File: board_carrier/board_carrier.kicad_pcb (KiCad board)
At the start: 2 copper layers, 40 x 36.5 mm, 13 parts, among them J1 Conn_01x08, J2 Conn_01x08, J3 Conn_02x06_Top_Bottom, U1 TJA1051T-3, U2 LM78M05_TO252

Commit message: carrier mods
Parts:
- removed the REF** at (45.0, 66.8)
- added REF**: OSHW-Logo_11.4x12mm_SilkScreen, Symbol:OSHW-Logo_11.4x12mm_SilkScreen, B.Cu at (60.0, 83.0)
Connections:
- J3 pad 10: Net-(J3-Pad10) -> /LSU_Un
- J3 pad 7: /LSU_Vm -> Net-(J3-Pad7)
- J3 pad 8: /LSU_Rtrim -> /LSU_Vm
- J3 pad 9: /LSU_Un -> /LSU_Rtrim
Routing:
- net /LSU_Vm: track 26.2 -> 32.2 mm
- net /LSU_Rtrim: track 35.3 -> 40.0 mm
- net /LSU_Un: track 43.2 -> 47.9 mm
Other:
- board text added: "5v"
- board text added: "Boot0"
- board text added: "CAN RX"
- board text added: "CAN TX"
- board text added: "Heater-"
- board text added: "Ip 1"
- board text added: "RX"
- board text added: "Rtrim 5"
- board text added: "TX"
- board text added: "Un 6"
- board text added: "Vm 2"
- board text added: "nRESET"

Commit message: carrier probably done
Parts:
- added JLCTAG**: JLC_PCB_TAG, rusefi:JLC_PCB_TAG, F.Cu at (50.6, 56.4)
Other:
- board text added: "v1.0"
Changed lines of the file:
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@@
   (general
     (thickness 1.6)
-    (drawings 46)
+    (drawings 47)
     (tracks 123)
     (zones 0)
-    (modules 13)
+    (modules 14)
     (nets 21)
   )
@@
     (add_net "Net-(J3-Pad5)")
     (add_net "Net-(J3-Pad7)")
+  )
+  (module rusefi:JLC_PCB_TAG (layer F.Cu)
+    (at 50.6 56.4)
+    (fp_text reference JLCTAG** (at 0 0.5) (layer F.SilkS) hide
+      (effects (font (size 1 1) (thickness 0.15)))
+    )
+    (fp_text value JLC_PCB_TAG (at 0 -0.5) (layer F.Fab)
+      (effects (font (size 1 1) (thickness 0.15)))
+    )
+    (fp_line (start 0 0) (end 19.05 0) (layer F.SilkS) (width 0.12))
+    (fp_line (start 19.05 0) (end 19.05 3.81) (layer F.SilkS) (width 0.12))
+    (fp_line (start 19.05 3.81) (end 0 3.81) (layer F.SilkS) (width 0.12))
+    (fp_line (start 0 3.81) (end 0 0) (layer F.SilkS) (width 0.12))
+    (fp_text user "JLC Order Number" (at 9.525 0.635) (layer F.SilkS)
+      (effects (font (size 0.762 0.762) (thickness 0.127)))
+    )
+    (fp_text user JLCJLCJLCJLC (at 9.525 2.54) (layer F.SilkS)
+      (effects (font (size 1.524 1.524) (thickness 0.2032)))
+    )
   )
   (module Symbol:OSHW-Logo_11.4x12mm_SilkScreen (layer B.Cu)
@@
     )
   )
+  (gr_text v1.0 (at 44.4 66.2) (layer B.SilkS)
+    (effects (font (size 1 1) (thickness 0.15)) (justify mirror))
+  )
   (gr_text 5v (at 45 71.2) (layer B.SilkS)

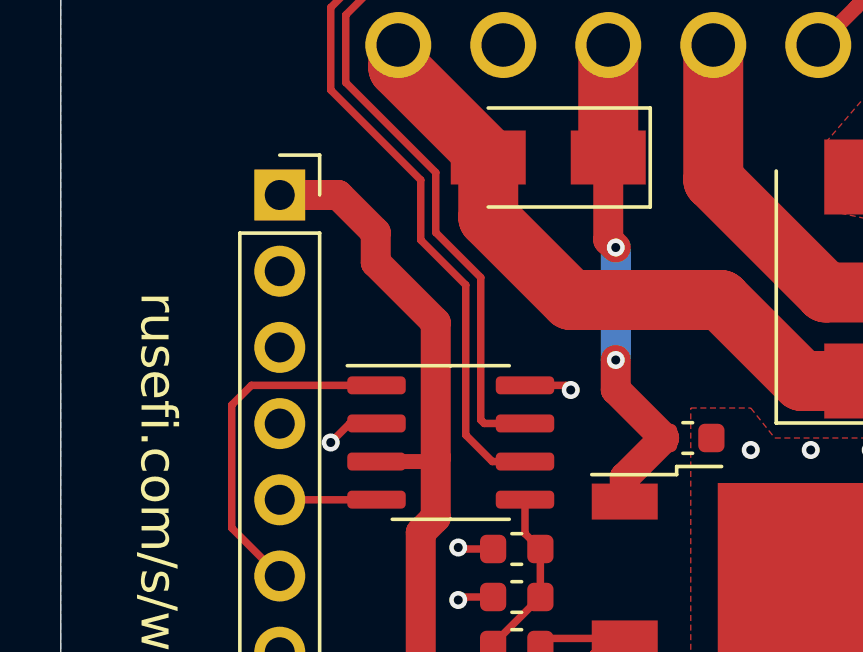
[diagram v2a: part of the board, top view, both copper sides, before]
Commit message: add CAN caps, solid reg pad
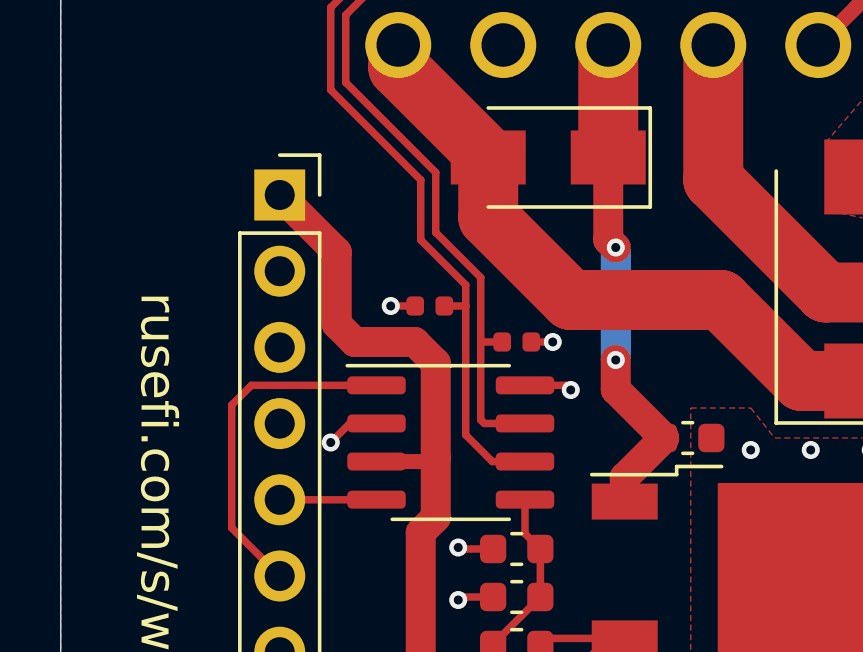
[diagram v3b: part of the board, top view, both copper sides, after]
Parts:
- added C4: 47p, Capacitor_SMD:C_0402_1005Metric, F.Cu at (55.2, 75.9)
- added C5: 47p, Capacitor_SMD:C_0402_1005Metric, F.Cu at (52.3, 74.7)
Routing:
- net GND: track 5.76 -> 7.29 mm, vias 16 -> 18
- net /CAN_L: track 21.6 -> 22.4 mm
- net /CAN_H: track 23.2 -> 23.9 mm

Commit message: moar caps
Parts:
- added C10: 10u, Capacitor_SMD:C_1206_3216Metric, F.Cu at (61.7, 77.1)
- added C6: 22u, Capacitor_SMD:C_0805_2012Metric, F.Cu at (58.8, 89.8)
- added C7: 10u, Capacitor_SMD:C_1206_3216Metric, F.Cu at (53.2, 72.4)
- added C8: 10u, Capacitor_SMD:C_1206_3216Metric, F.Cu at (53.2, 70.0)
- added C9: 10u, Capacitor_SMD:C_1206_3216Metric, F.Cu at (53.2, 74.8)
- moved C5 3.59 mm to (53.8, 78.0)
- moved D1 3.06 mm to (65.4, 71.2), turned to 0 degrees
- moved D2 2.43 mm to (58.2, 71.2), turned to 270 degrees
- moved C4 2.15 mm to (55.8, 78.0)
- moved C3 2.09 mm to (55.7, 86.4)
- moved R1 2.09 mm to (55.7, 88.0)
- moved R2 2.09 mm to (55.7, 84.8)
- moved U1 2.03 mm to (53.0, 81.3)
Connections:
- J1 pad 3: /UART_TX -> (no net)
- J1 pad 4: /UART_RX -> (no net)
- J1 pad 7: /nRESET -> (no net)
- J1 pad 8: /Boot0 -> (no net)
- J3 pad 5: Net-(J3-Pad5) -> (no net)
- J3 pad 7: Net-(J3-Pad7) -> (no net)
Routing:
- net 12V_RAW: track 22.1 -> 0.00 mm
- net /CAN_L: track 22.4 -> 27.4 mm
- net /CAN_H: track 23.9 -> 28.4 mm
- net /LSU_Heater+: track 16.5 -> 19.6 mm
- net GND: track 7.29 -> 9.40 mm, vias 18 -> 28
- net /CAN_TX: track 11.5 -> 9.37 mm
- net /CAN_RX: track 3.23 -> 4.17 mm
- added copper zone on F.Cu, net 12V_RAW

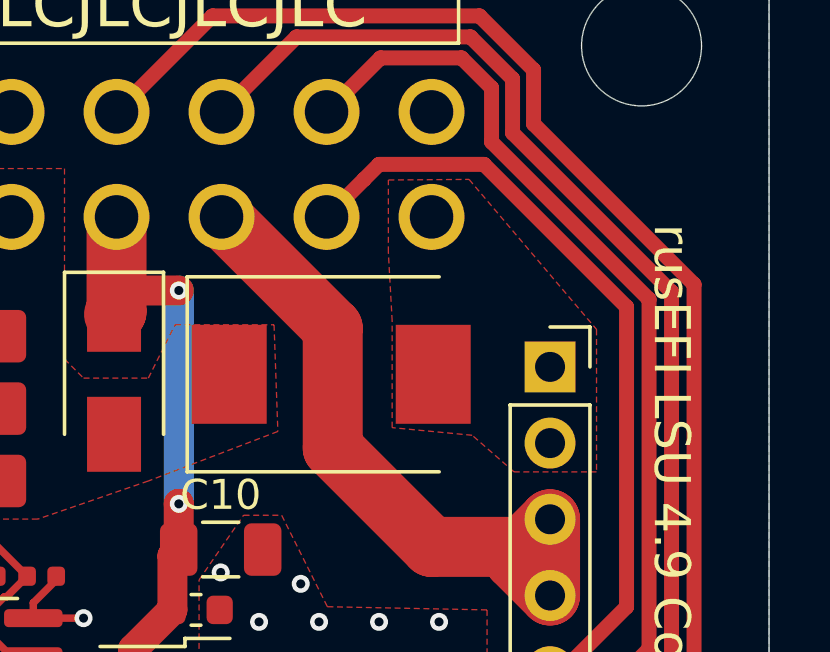
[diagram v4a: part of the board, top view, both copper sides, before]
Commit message: more stitching
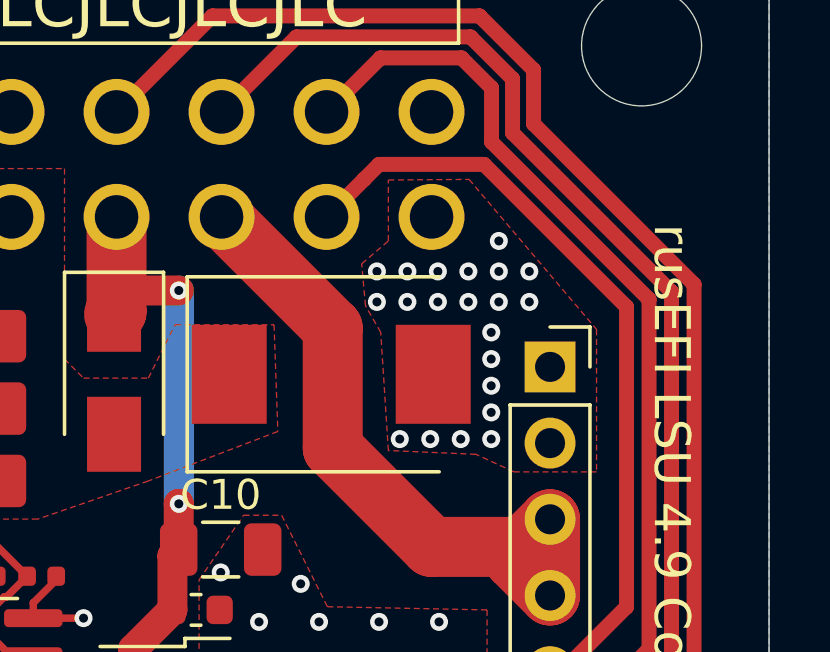
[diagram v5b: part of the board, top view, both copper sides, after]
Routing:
- net GND: vias 28 -> 49
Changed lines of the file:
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@@
     (thickness 1.6)
     (drawings 46)
-    (tracks 156)
+    (tracks 177)
     (zones 0)
     (modules 21)
@@
     (uvia_drill 0.3)
     (add_net +5V)
+    (add_net /Boot0)
     (add_net /CAN_H)
     (add_net /CAN_L)
@@
     (add_net /LSU_Un)
     (add_net /LSU_Vm)
+    (add_net /UART_RX)
+    (add_net /UART_TX)
+    (add_net /nRESET)
     (add_net 12V_RAW)
     (add_net GND)
     (add_net "Net-(C3-Pad1)")
+    (add_net "Net-(J3-Pad5)")
+    (add_net "Net-(J3-Pad7)")
+  )
+  (module Diode_SMD:D_SMA (layer F.Cu)
+    (at 58.166 71.247 270)
+    (descr "Diode SMA (DO-214AC)")
+    (tags "Diode SMA (DO-214AC)")
+    (attr smd)
+    (fp_text reference D2 (at 0 -2.5 90) (layer F.SilkS) hide
+      (effects (font (size 1 1) (thickness 0.15)))
+    )
+    (fp_text value D_Schottky (at 0 2.6 90) (layer F.Fab)
+      (effects (font (size 1 1) (thickness 0.15)))
+    )
+    (fp_line (start -3.4 -1.65) (end 2 -1.65) (layer F.SilkS) (width 0.12))
+    (fp_line (start -3.4 1.65) (end 2 1.65) (layer F.SilkS) (width 0.12))
+    (fp_line (start -0.64944 0.00102) (end 0.50118 -0.79908) (layer F.Fab) (width 0.1))
+    (fp_line (start -0.64944 0.00102) (end 0.50118 0.75032) (layer F.Fab) (width 0.1))
+    (fp_line (start 0.50118 0.75032) (end 0.50118 -0.79908) (layer F.Fab) (width 0.1))
+    (fp_line (start -0.64944 -0.79908) (end -0.64944 0.80112) (layer F.Fab) (width 0.1))
+    (fp_line (start 0.50118 0.00102) (end 1.4994 0.00102) (layer F.Fab) (width 0.1))
+    (fp_line (start -0.64944 0.00102) (end -1.55114 0.00102) (layer F.Fab) (width 0.1))
+    (fp_line (start -3.5 1.75) (end -3.5 -1.75) (layer F.CrtYd) (width 0.05))
+    (fp_line (start 3.5 1.75) (end -3.5 1.75) (layer F.CrtYd) (width 0.05))
+    (fp_line (start 3.5 -1.75) (end 3.5 1.75) (layer F.CrtYd) (width 0.05))
+    (fp_line (start -3.5 -1.75) (end 3.5 -1.75) (layer F.CrtYd) (width 0.05))
+    (fp_line (start 2.3 -1.5) (end -2.3 -1.5) (layer F.Fab) (width 0.1))
+    (fp_line (start 2.3 -1.5) (end 2.3 1.5) (layer F.Fab) (width 0.1))
+    (fp_line (start -2.3 1.5) (end -2.3 -1.5) (layer F.Fab) (width 0.1))
+    (fp_line (start 2.3 1.5) (end -2.3 1.5) (layer F.Fab) (width 0.1))
+    (fp_line (start -3.4 -1.65) (end -3.4 1.65) (layer F.SilkS) (width 0.12))
+    (fp_text user %R (at 0 -2.5 90) (layer F.Fab) hide
+      (effects (font (size 1 1) (thickness 0.15)))
+    )
+    (pad 2 smd rect (at 2 0 270) (size 2.5 1.8) (layers F.Cu F.Paste F.Mask)
+      (net 4 12V_RAW))
+    (pad 1 smd rect (at -2 0 270) (size 2.5 1.8) (layers F.Cu F.Paste F.Mask)
+      (net 9 /LSU_Heater+))
+    (model ${KISYS3DMOD}/Diode_SMD.3dshapes/D_SMA.wrl
+      (at (xyz 0 0 0))
+      (scale (xyz 1 1 1))
+      (rotate (xyz 0 0 0))
+    )
   )
   (module Capacitor_SMD:C_1206_3216Metric (layer F.Cu)
@@
     )
   )
-  (module Diode_SMD:D_SMA (layer F.Cu)
-    (at 58.166 71.247 270)
-    (descr "Diode SMA (DO-214AC)")
-    (tags "Diode SMA (DO-214AC)")
-    (attr smd)
-    (fp_text reference D2 (at 0 -2.5 90) (layer F.SilkS) hide
-      (effects (font (size 1 1) (thickness 0.15)))
-    )
-    (fp_text value D_Schottky (at 0 2.6 90) (layer F.Fab)
-      (effects (font (size 1 1) (thickness 0.15)))
-    )
-    (fp_line (start -3.4 -1.65) (end 2 -1.65) (layer F.SilkS) (width 0.12))
-    (fp_line (start -3.4 1.65) (end 2 1.65) (layer F.SilkS) (width 0.12))
-    (fp_line (start -0.64944 0.00102) (end 0.50118 -0.79908) (layer F.Fab) (width 0.1))
-    (fp_line (start -0.64944 0.00102) (end 0.50118 0.75032) (layer F.Fab) (width 0.1))
-    (fp_line (start 0.50118 0.75032) (end 0.50118 -0.79908) (layer F.Fab) (width 0.1))
-    (fp_line (start -0.64944 -0.79908) (end -0.64944 0.80112) (layer F.Fab) (width 0.1))
-    (fp_line (start 0.50118 0.00102) (end 1.4994 0.00102) (layer F.Fab) (width 0.1))
-    (fp_line (start -0.64944 0.00102) (end -1.55114 0.00102) (layer F.Fab) (width 0.1))
-    (fp_line (start -3.5 1.75) (end -3.5 -1.75) (layer F.CrtYd) (width 0.05))
-    (fp_line (start 3.5 1.75) (end -3.5 1.75) (layer F.CrtYd) (width 0.05))
-    (fp_line (start 3.5 -1.75) (end 3.5 1.75) (layer F.CrtYd) (width 0.05))
-    (fp_line (start -3.5 -1.75) (end 3.5 -1.75) (layer F.CrtYd) (width 0.05))
-    (fp_line (start 2.3 -1.5) (end -2.3 -1.5) (layer F.Fab) (width 0.1))
-    (fp_line (start 2.3 -1.5) (end 2.3 1.5) (layer F.Fab) (width 0.1))
-    (fp_line (start -2.3 1.5) (end -2.3 -1.5) (layer F.Fab) (width 0.1))
-    (fp_line (start 2.3 1.5) (end -2.3 1.5) (layer F.Fab) (width 0.1))
-    (fp_line (start -3.4 -1.65) (end -3.4 1.65) (layer F.SilkS) (width 0.12))
-    (fp_text user %R (at 0 -2.5 90) (layer F.Fab) hide
-      (effects (font (size 1 1) (thickness 0.15)))
-    )
-    (pad 2 smd rect (at 2 0 270) (size 2.5 1.8) (layers F.Cu F.Paste F.Mask)
-      (net 4 12V_RAW))
-    (pad 1 smd rect (at -2 0 270) (size 2.5 1.8) (layers F.Cu F.Paste F.Mask)
-      (net 9 /LSU_Heater+))
-    (model ${KISYS3DMOD}/Diode_SMD.3dshapes/D_SMA.wrl
-      (at (xyz 0 0 0))
-      (scale (xyz 1 1 1))
-      (rotate (xyz 0 0 0))
-    )
-  )
   (module Diode_SMD:D_SMC (layer F.Cu)
     (at 65.405 71.247)
@@
   (via (at 53.086 70.612) (size 0.6) (drill 0.3) (layers F.Cu B.Cu) (net 1))
   (via (at 53.086 69.342) (size 0.6) (drill 0.3) (layers F.Cu B.Cu) (net 1))
+  (via (at 67.945 67.818) (size 0.6) (drill 0.3) (layers F.Cu B.Cu) (net 1))
+  (via (at 68.961 67.818) (size 0.6) (drill 0.3) (layers F.Cu B.Cu) (net 1))
+  (via (at 69.977 67.818) (size 0.6) (drill 0.3) (layers F.Cu B.Cu) (net 1))
+  (via (at 70.993 67.818) (size 0.6) (drill 0.3) (layers F.Cu B.Cu) (net 1))
+  (via (at 70.993 66.802) (size 0.6) (drill 0.3) (layers F.Cu B.Cu) (net 1))
+  (via (at 72.009 67.818) (size 0.6) (drill 0.3) (layers F.Cu B.Cu) (net 1))
+  (via (at 72.009 68.834) (size 0.6) (drill 0.3) (layers F.Cu B.Cu) (net 1))
+  (via (at 70.993 68.834) (size 0.6) (drill 0.3) (layers F.Cu B.Cu) (net 1))
+  (via (at 69.977 68.834) (size 0.6) (drill 0.3) (layers F.Cu B.Cu) (net 1))
+  (via (at 68.961 68.834) (size 0.6) (drill 0.3) (layers F.Cu B.Cu) (net 1))
+  (via (at 67.945 68.834) (size 0.6) (drill 0.3) (layers F.Cu B.Cu) (net 1))
+  (via (at 70.739 69.85) (size 0.6) (drill 0.3) (layers F.Cu B.Cu) (net 1))
+  (via (at 70.739 70.739) (size 0.6) (drill 0.3) (layers F.Cu B.Cu) (net 1))
+  (via (at 70.739 71.628) (size 0.6) (drill 0.3) (layers F.Cu B.Cu) (net 1))
+  (via (at 70.739 72.517) (size 0.6) (drill 0.3) (layers F.Cu B.Cu) (net 1))
+  (via (at 70.739 73.406) (size 0.6) (drill 0.3) (layers F.Cu B.Cu) (net 1))
+  (via (at 69.723 73.406) (size 0.6) (drill 0.3) (layers F.Cu B.Cu) (net 1))
+  (via (at 68.707 73.406) (size 0.6) (drill 0.3) (layers F.Cu B.Cu) (net 1))
+  (via (at 67.691 73.406) (size 0.6) (drill 0.3) (layers F.Cu B.Cu) (net 1))
+  (via (at 66.929 67.818) (size 0.6) (drill 0.3) (layers F.Cu B.Cu) (net 1))
+  (via (at 66.929 68.834) (size 0.6) (drill 0.3) (layers F.Cu B.Cu) (net 1))
   (segment (start 58.0125 86.5675) (end 58.0125 88) (width 1) (layer F.Cu) (net 2))
   (segment (start 58.8 85.78) (end 58.0125 86.5675) (width 1) (layer F.Cu) (net 2))
@@
     (polygon
       (pts
-        (xy 74.25 69.75) (xy 74.25 74.5) (xy 71.5 74.5) (xy 70.104 73.279) (xy 67.437 73.025)
-        (xy 67.437 69.469) (xy 67.31 67.183) (xy 67.31 64.77) (xy 70 64.75)
+        (xy 74.25 69.75) (xy 74.25 74.5) (xy 71.5 74.5) (xy 70.231 73.914) (xy 67.31 73.787)
+        (xy 67.056 69.847941) (xy 66.548 68.961) (xy 66.421 67.564) (xy 67.31 66.802) (xy 67.31 64.77)
+        (xy 70 64.75)
       )
     )

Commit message: version text
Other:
- board text added: "v1.1"
- board text removed: "v1.0"
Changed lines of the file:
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@@
   )
   (setup
-    (last_trace_width 0.5)
+    (last_trace_width 0.25)
     (user_trace_width 0.25)
     (user_trace_width 0.5)
@@
     (uvia_drill 0.3)
     (add_net +5V)
-    (add_net /Boot0)
     (add_net /CAN_H)
     (add_net /CAN_L)
@@
     (add_net /LSU_Un)
     (add_net /LSU_Vm)
-    (add_net /UART_RX)
-    (add_net /UART_TX)
-    (add_net /nRESET)
     (add_net 12V_RAW)
     (add_net GND)
     (add_net "Net-(C3-Pad1)")
-    (add_net "Net-(J3-Pad5)")
-    (add_net "Net-(J3-Pad7)")
   )
   (module Diode_SMD:D_SMA (layer F.Cu)
@@
     (effects (font (size 1.2 1.1) (thickness 0.2)) (justify mirror))
   )
-  (gr_text v1.0 (at 44.4 66.2) (layer B.SilkS)
+  (gr_text v1.1 (at 44.4 66.2) (layer B.SilkS)
     (effects (font (size 1 1) (thickness 0.15)) (justify mirror))
   )

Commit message: tweak pour
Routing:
- net GND: vias 49 -> 47
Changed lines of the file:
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@@
     (thickness 1.6)
     (drawings 46)
-    (tracks 177)
+    (tracks 175)
     (zones 0)
     (modules 21)
@@
   (via (at 69.723 73.406) (size 0.6) (drill 0.3) (layers F.Cu B.Cu) (net 1))
   (via (at 68.707 73.406) (size 0.6) (drill 0.3) (layers F.Cu B.Cu) (net 1))
-  (via (at 67.691 73.406) (size 0.6) (drill 0.3) (layers F.Cu B.Cu) (net 1))
-  (via (at 66.929 67.818) (size 0.6) (drill 0.3) (layers F.Cu B.Cu) (net 1))
-  (via (at 66.929 68.834) (size 0.6) (drill 0.3) (layers F.Cu B.Cu) (net 1))
+  (via (at 67.183 67.818) (size 0.6) (drill 0.3) (layers F.Cu B.Cu) (net 1))
   (segment (start 58.0125 86.5675) (end 58.0125 88) (width 1) (layer F.Cu) (net 2))
   (segment (start 58.8 85.78) (end 58.0125 86.5675) (width 1) (layer F.Cu) (net 2))
@@
     (polygon
       (pts
-        (xy 74.25 69.75) (xy 74.25 74.5) (xy 71.5 74.5) (xy 70.231 73.914) (xy 67.31 73.787)
-        (xy 67.056 69.847941) (xy 66.548 68.961) (xy 66.421 67.564) (xy 67.31 66.802) (xy 67.31 64.77)
-        (xy 70 64.75)
+        (xy 74.25 69.75) (xy 74.25 74.5) (xy 71.5 74.5) (xy 70.231 73.914) (xy 68.072 73.914)
+        (xy 67.183 73.025) (xy 67.183 69.215) (xy 66.675 68.707) (xy 66.675 67.437) (xy 67.31 66.802)
+        (xy 67.31 64.77) (xy 70 64.75)
       )
     )
@@
     (polygon
       (pts
-        (xy 56.515 70.739) (xy 57.15 71.374) (xy 59.309 71.374) (xy 60.198 69.596) (xy 63.5 69.596)
-        (xy 63.627 73.152) (xy 59.309 74.803) (xy 55.626 76.073) (xy 53.848 76.073) (xy 53.848 68.707)
+        (xy 56.515 70.739) (xy 57.15 71.374) (xy 59.309 71.374) (xy 60.325 69.596) (xy 63.246 69.596)
+        (xy 63.246 73.152) (xy 59.69 74.803) (xy 55.753 76.073) (xy 53.848 76.073) (xy 53.848 68.707)
         (xy 53.721 68.58) (xy 49.784 68.58) (xy 49.784 64.77) (xy 52.705 64.389) (xy 56.515 64.389)
       )
